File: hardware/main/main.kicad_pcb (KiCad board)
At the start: 2 copper layers, 75 x 75 mm, 62 parts, among them J1 Conn_01x10, J10 Conn_01x02, J11 Conn_01x02, J2 Conn_01x10, J3 Conn_01x02, J4 USB_B_Micro, J5 Conn_01x04, J6 Conn_01x03, J7 Conn_01x02, J8 Conn_01x03, J9 Conn_01x02, K1 G6SU-2, K2 G6SU-2, K3 G6SU-2, K4 G6SU-2, K5 G6SU-2, K6 G6SU-2, K7 G6SU-2, K8 G6SU-2, SW1 Rotary_Encoder_Switch, U1 NCV7726B, U10 SP3485EN, U2 MAX98357A, U3 MOC3043M, U4 SP3485EN, U5 E73-2G4M08S1C-52840, U6 BME680, U7 TPS82130, U8 D203S, U9 UG-2864ASWPG01

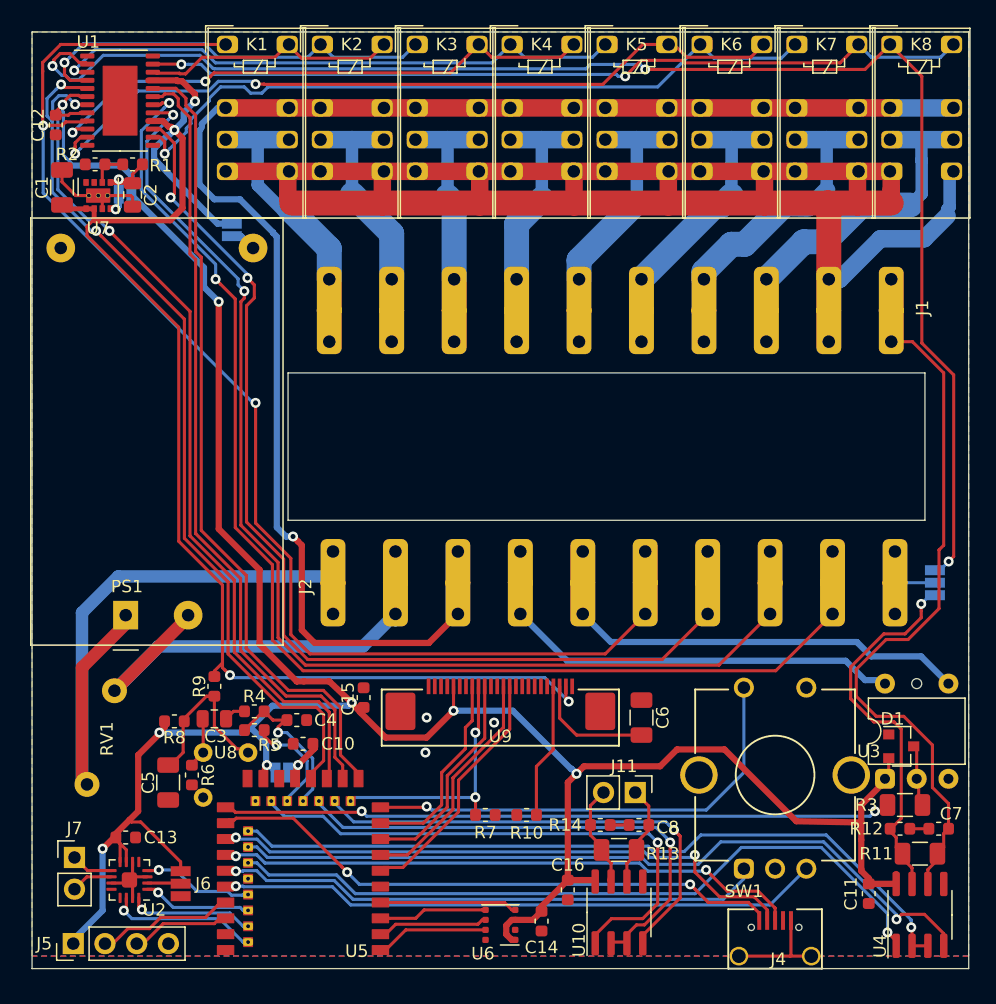
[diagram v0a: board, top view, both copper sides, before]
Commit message: Update main board to use LIN
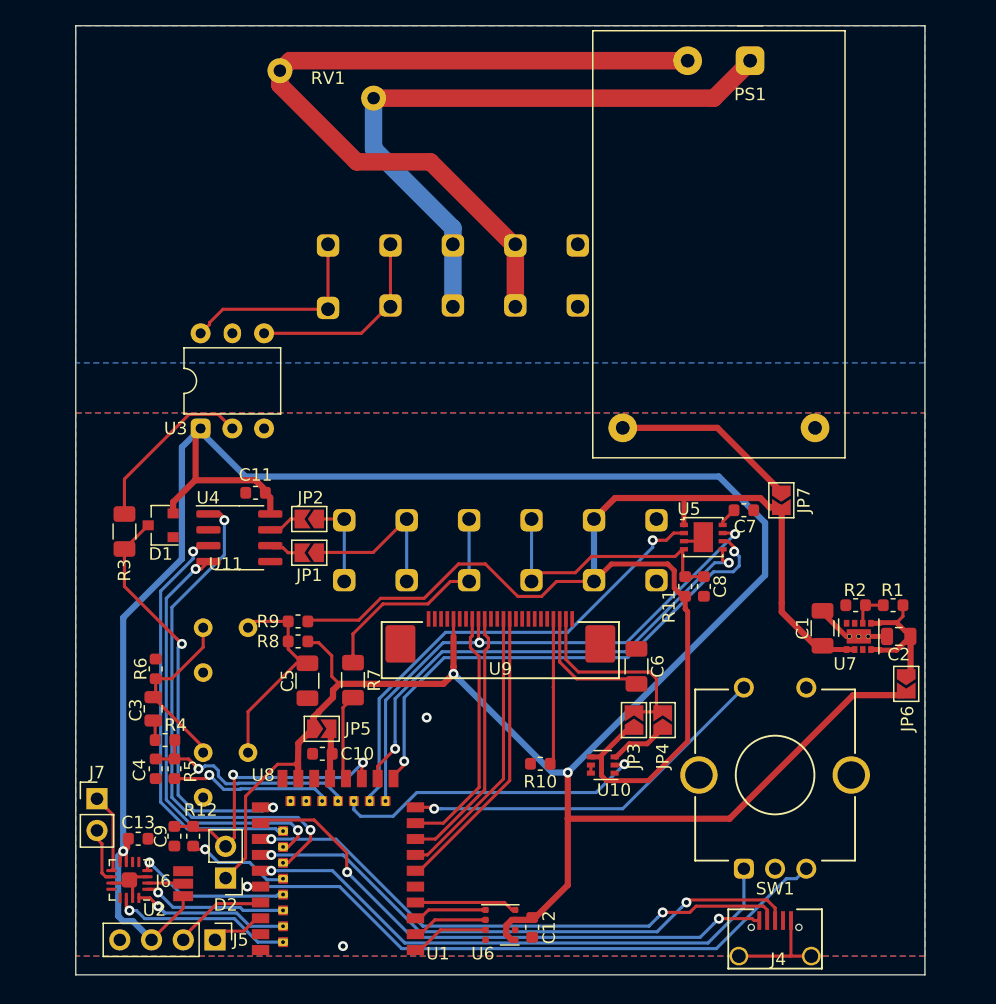
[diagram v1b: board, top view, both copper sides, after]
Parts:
- removed C14, C15, C16: 100n, Capacitor_SMD:C_0603_1608Metric
- removed J10, J3, J9: Conn_01x02, RoomControl:Jumper2
- removed J11: Conn_01x02, Connector_PinHeader_2.54mm:PinHeader_1x02_P2.54mm_Vertical
- removed J8: Conn_01x03, RoomControl:Jumper3
- removed K1, K2, K3, K4, K5, K6, K7, K8: G6SU-2, RoomControl:Relay_DPDT_Omron_G6SU-2
- removed R13: 120R, Resistor_SMD:R_1206_3216Metric
- removed R14: 120R, Resistor_SMD:R_0603_1608Metric
- removed the U1 at (69.5, 68.0)
- added C9: 100n, Capacitor_SMD:C_0603_1608Metric, F.Cu at (73.9, 126.9)
- added D2: D_Photo, Connector_PinHeader_2.54mm:PinHeader_1x02_P2.54mm_Vertical, F.Cu at (78.0, 130.2)
- added JP1: SolderJumper_2_Open, RoomControl:Jumper2Triangular, F.Cu at (84.7, 104.2)
- added JP2: SolderJumper_2_Open, RoomControl:Jumper2Triangular, F.Cu at (84.7, 101.5)
- added JP3: SolderJumper_2_Open, RoomControl:Jumper2Triangular, F.Cu at (110.7, 117.6)
- added JP4: SolderJumper_2_Open, RoomControl:Jumper2Triangular, F.Cu at (113.0, 117.6)
- added JP5: SolderJumper_2_Open, RoomControl:Jumper2Triangular, F.Cu at (85.7, 118.3)
- added JP6: SolderJumper_2_Open, RoomControl:Jumper2Triangular, F.Cu at (132.5, 114.7)
- added JP7: SolderJumper_2_Open, RoomControl:Jumper2Triangular, F.Cu at (122.5, 100.0)
- added U11: D203S, RoomControl:D203S, F.Cu at (78.0, 112.0)
- added U5: NCV7428MW, Package_DFN_QFN:DFN-8-1EP_3x3mm_P0.65mm_EP1.55x2.4mm, F.Cu at (116.2, 103.0)
- C8: value 100n -> 1n
- J1: value Conn_01x10 -> Conn_01x06; footprint RoomControl:WAGO-236-410 -> RoomControl:Wago_236-406; moved to B.Cu
- J2: value Conn_01x10 -> Conn_01x05; footprint RoomControl:WAGO-236-410 -> RoomControl:Wago_236-405; moved to B.Cu
- PS1: footprint Converter_ACDC:Converter_ACDC_HiLink_HLK-PMxx -> RoomControl:Converter_ACDC_HiLink_HLK-PMxx
- R11: value 120R -> 1k; footprint Resistor_SMD:R_1206_3216Metric -> Resistor_SMD:R_0603_1608Metric
- R12: value 120R -> 100k
- R7: value 33k -> 100k; footprint Resistor_SMD:R_0603_1608Metric -> Resistor_SMD:R_1206_3216Metric
- U10: value SP3485EN -> DCX114YU; footprint Package_SO:SOIC-8_3.9x4.9mm_P1.27mm -> Package_TO_SOT_SMD:SOT-363_SC-70-6
- moved C12 74.7 mm to (102.5, 134.2)
- moved C2 70.8 mm to (131.9, 110.9), turned to 180 degrees
- moved C1 70.4 mm to (125.8, 110.2)
- moved R1 70.4 mm to (131.4, 108.4)
- moved R2 70.4 mm to (128.4, 108.4)
- moved U7 70.4 mm to (128.7, 110.9)
- moved PS1 66.9 mm to (120.0, 64.8), turned to 270 degrees
- moved R3 66.2 mm to (69.9, 102.5), turned to 90 degrees
- moved U4 62.3 mm to (79.1, 103.0), turned to 0 degrees
- moved D1 61.9 mm to (72.8, 102.0), turned to 180 degrees
- moved U3 61.6 mm to (76.0, 94.2)
- moved C11 58.7 mm to (80.4, 99.4), turned to 0 degrees
- moved R12 56.6 mm to (75.4, 126.9), turned to 270 degrees
- moved RV1 55.3 mm to (86.1, 66.7), turned to 180 degrees
- moved J1 48.9 mm to (87.5, 104.0)
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- renumbered U5 to U1
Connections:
- net DET_COMP renamed MD_COMP
- net DET_DS renamed MD_DS
- C7 pad 1: Net-(C7-Pad1) -> GND
- C7 pad 2: A -> Net-(C7-Pad2)
- C8 pad 1: Net-(C8-Pad1) -> GND
- C8 pad 2: Net-(C8-Pad2) -> LIN
- D1 pad 3: Net-(D1-Pad3) -> H
- J1 pad 1: A -> RS485_B
- J1 pad 2: L2 -> RS485_A
- J1 pad 3: S1 -> IN
- J1 pad 4: S2 -> LIN
- J1 pad 5: S3 -> +12V
- J1 pad 6: S4 -> GND
- J2 pad 1: L -> H1
- J2 pad 2: N -> H2
- J2 pad 3: PE -> L
- J2 pad 4: H1 -> N
- J2 pad 5: H2 -> PE
- J5 pad 1: +3V3 -> SWDCLK
- J5 pad 3: SWDCLK -> +3V3
- R11 pad 1: B -> LIN
- R11 pad 2: A -> +12V
- R12 pad 1: B -> BS_COMP
- R12 pad 2: Net-(C7-Pad1) -> BS_DS
- R3 pad 2: Net-(D1-Pad3) -> Net-(R3-Pad2)
- R7 pad 1: DISP_RES -> IN
- R7 pad 2: GND -> IN_P
- U1 pad 11: R_SCLK -> LIN_TX
- U1 pad 12: DISP_RES -> RESET
- U1 pad 13: R_CS -> LIN_RX
- U1 pad 14: RS485_2_TX -> LIN_EN
- U1 pad 15: R_MISO -> BS_COMP
- U1 pad 16: RS485_2_DE -> EN_12V
- U1 pad 17: R_MOSI -> IN_P
- U1 pad 22: RS485_2_RX -> Net-(U1-Pad22)
- U1 pad 34: Net-(U5-Pad34) -> BS_DS
- U10 pad 1: RS485_2_RX -> GND
- U10 pad 2: RS485_2_DE -> EN_12V
- U10 pad 3: RS485_2_DE -> Net-(JP4-Pad1)
- U10 pad 4: RS485_2_TX -> +12V
- U10 pad 5: GND -> Net-(U10-Pad5)
- U10 pad 6: Net-(C8-Pad2) -> Net-(U10-Pad5)
- U2 pad 6: GND -> Net-(U2-Pad6)
- U3 pad 2: Net-(D1-Pad3) -> Net-(R3-Pad2)
- U4 pad 6: A -> Net-(JP1-Pad2)
- U4 pad 7: B -> Net-(JP2-Pad2)
- U9 pad 23: +12V -> Net-(JP3-Pad2)
- U9 pad 9: DISP_RES -> RESET
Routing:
- net L2: track 143.2 -> 0.00 mm
- net PE: track 119.9 -> 0.00 mm, vias 1 -> 0
- net R1: track 118.7 -> 0.00 mm, vias 3 -> 0
- net R9: track 103.5 -> 0.00 mm, vias 2 -> 0
- net R12: track 97.8 -> 0.00 mm, vias 2 -> 0
- net R11: track 91.4 -> 0.00 mm, vias 2 -> 0
- net R10: track 82.0 -> 0.00 mm, vias 2 -> 0
- net R_MOSI: track 69.4 -> 0.00 mm, vias 2 -> 0
- net R_MISO: track 68.5 -> 0.00 mm, vias 2 -> 0
- net R2: track 66.9 -> 0.00 mm, vias 2 -> 0
- net R_SCLK: track 65.2 -> 0.00 mm
- net R_CS: track 64.2 -> 0.00 mm
- net R4: track 61.5 -> 0.00 mm, vias 2 -> 0
- net R3: track 58.3 -> 0.00 mm, vias 1 -> 0
- net A: track 55.1 -> 0.00 mm
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- added copper zone on B.Cu, net PE
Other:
- board size 75 x 75 mm -> 68 x 76 mm
- net class HiVolt removed
- net class Mains added: clearance 1, trace_width 0.25, via_dia 0.8, via_drill 0.4
- net class PE removed
- board text added: "12V"
- board text added: "A"
- board text added: "B"
- board text added: "GND"
- board text added: "H"
- board text added: "IN"
- board text added: "L"
- board text added: "LIN"
- board text added: "N"
- board text added: "PE"
- board text added: "RS485"

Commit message: Add backup battery and 32768Hz crystal
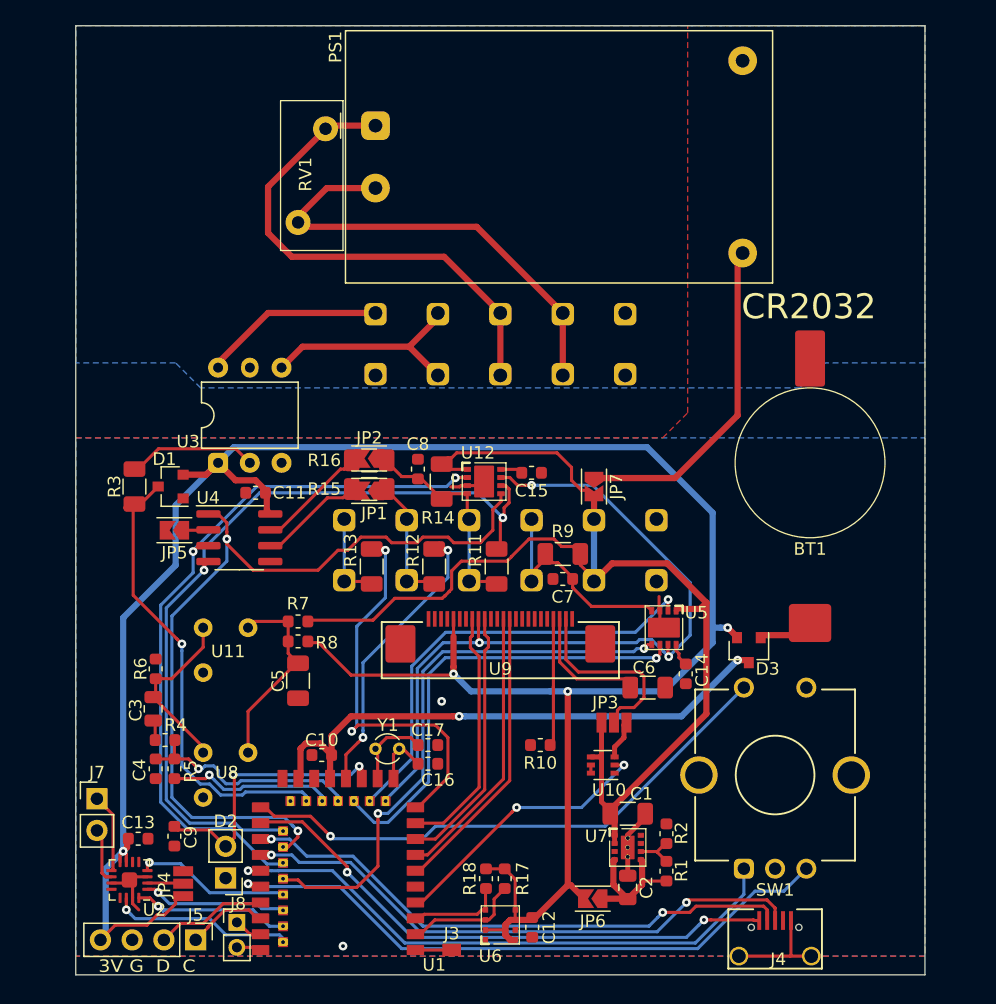
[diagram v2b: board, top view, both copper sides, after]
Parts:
- removed J6: Conn_01x03, RoomControl:Jumper3
- removed the R11 at (114.8, 106.9)
- added BT1: Battery_Cell, RoomControl:Battery_2032, F.Cu at (124.8, 97.0)
- added C14: 100n, Capacitor_SMD:C_0603_1608Metric, F.Cu at (114.8, 113.9)
- added C15: 100n, Capacitor_SMD:C_0603_1608Metric, F.Cu at (102.5, 97.8)
- added C16: 12p, Capacitor_SMD:C_0603_1608Metric, F.Cu at (94.2, 121.1)
- added C17: 12p, Capacitor_SMD:C_0603_1608Metric, F.Cu at (94.2, 119.6)
- added D3: BAS40-05/BAT54C, Package_TO_SOT_SMD:SOT-23, F.Cu at (119.9, 112.0)
- added J3: Conn_01x01, RoomControl:Pad, F.Cu at (96.1, 136.0)
- added J8: Conn_01x02, Connector_PinHeader_2.00mm:PinHeader_1x02_P2.00mm_Vertical, F.Cu at (78.9, 133.8)
- added R13: 33k, Resistor_SMD:R_1206_3216Metric, F.Cu at (89.7, 105.3)
- added R14: 1k, Resistor_SMD:R_1206_3216Metric, F.Cu at (95.3, 98.5)
- added R15: 120R, Resistor_SMD:R_1206_3216Metric, F.Cu at (89.5, 99.1)
- added R16: 120R, Resistor_SMD:R_1206_3216Metric, F.Cu at (89.5, 96.8)
- added R17: 4k7, Resistor_SMD:R_0603_1608Metric, F.Cu at (100.3, 130.3)
- added R18: 4k7, Resistor_SMD:R_0603_1608Metric, F.Cu at (98.8, 130.3)
- added R7: 33k, Resistor_SMD:R_0603_1608Metric, F.Cu at (83.8, 109.7)
- added U12: NCV7428MW3, RoomControl:On_NCV7428MW, F.Cu at (98.7, 98.5)
- added Y1: 32768Hz, Crystal:Crystal_DS26_D2.0mm_L6.0mm_Vertical, F.Cu at (91.9, 119.9)
- C1, C5: value 10u/25V/7XR -> 10u/25V/X7R
- C2, C3: value 22u -> 22u/16V
- C6: value 10u/25V -> 10u/25V/X7R
- C7: value 100n -> 1n
- D1: value BAT54S -> BAS40-04/BAT54S
- JP1, JP2, JP5, JP6, JP7: footprint RoomControl:Jumper2Triangular -> RoomControl:Jumper2
- JP3, JP4: value SolderJumper_2_Open -> SolderJumper_3_Open; footprint RoomControl:Jumper2Triangular -> RoomControl:Jumper3
- PS1: footprint RoomControl:Converter_ACDC_HiLink_HLK-PMxx -> RoomControl:HiLink_HLK-PMxx
- R11: renamed from R7; value 100k -> 33k
- R12: value 100k -> 33k; footprint Resistor_SMD:R_0603_1608Metric -> Resistor_SMD:R_1206_3216Metric
- R6: value 47k -> 33k
- R8: value 33k -> 10k
- R9: value 33k -> 1k; footprint Resistor_SMD:R_0603_1608Metric -> Resistor_SMD:R_1206_3216Metric
- SW1: value Rotary_Encoder_Switch -> PEC12R-4217F-S0024; footprint RoomControl:ALPS-BOURNS-EC12 -> RoomControl:Bourns_PEC12R
- U3: footprint RoomControl:MOC3043 -> RoomControl:On_MOC3043
- U4: value SP3485EN -> SP3485
- U5: value NCV7428MW -> NCV7428MW3; footprint Package_DFN_QFN:DFN-8-1EP_3x3mm_P0.65mm_EP1.55x2.4mm -> RoomControl:On_NCV7428MW
- U6: footprint Package_LGA:Bosch_LGA-8_3x3mm_P0.8mm_ClockwisePinNumbering -> RoomControl:Bosch_BME680
- U7: footprint RoomControl:TPS82130 -> RoomControl:Texas_TPS82130
- moved JP4 40.6 mm to (74.6, 130.7), turned to 180 degrees
- moved PS1 30.4 mm to (90.0, 70.0), turned to 0 degrees
- moved JP6 30.4 mm to (107.4, 131.9), turned to 180 degrees
- moved C2 29.6 mm to (110.2, 131.0), turned to 90 degrees
- moved R12 29.0 mm to (94.7, 105.3), turned to 90 degrees
- moved R1 28.0 mm to (113.3, 129.7), turned to 90 degrees
- moved U7 25.1 mm to (110.2, 127.8), turned to 0 degrees
- moved C8 24.8 mm to (93.4, 97.5)
- moved J2 24.4 mm to (110.0, 87.5), turned to 90 degrees
- moved R2 23.8 mm to (113.3, 126.7), turned to 90 degrees
- moved R9 21.9 mm to (105.0, 104.3), turned to 0 degrees
- moved C1 21.5 mm to (110.2, 125.1), turned to 0 degrees
- moved JP5 19.8 mm to (73.9, 102.4), turned to 180 degrees
- moved C7 15.5 mm to (105.0, 106.3)
- moved JP7 15.0 mm to (107.5, 98.9)
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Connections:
- net BME_MOSI renamed BME_SDA
- net BME_SCK renamed BME_SCL
- C10 pad 1: GND -> Net-(C10-Pad1)
- C10 pad 2: Net-(C10-Pad2) -> GND
- C7 pad 1: GND -> LIN
- C7 pad 2: Net-(C7-Pad2) -> GND
- C8 pad 1: GND -> IN1_LIN2_RS485_B
- C8 pad 2: LIN -> GND
- C9 pad 2: BS_COMP -> BS
- D2 pad 1: +3V3 -> GND
- D2 pad 2: BS_COMP -> BS
- J1 pad 1: RS485_B -> IN3
- J1 pad 2: RS485_A -> IN2_RS485_A
- J1 pad 3: IN -> IN1_LIN2_RS485_B
- J2 pad 1: H1 -> PE
- J2 pad 2: H2 -> N
- J2 pad 4: N -> H2
- J2 pad 5: PE -> H1
- J5 pad 3: +3V3 -> GND
- J5 pad 4: GND -> +3V3
- JP1 pad 1: RS485_A -> IN2_RS485_A
- JP2 pad 1: RS485_B -> IN1_LIN2_RS485_B
- JP4 pad 1: Net-(JP4-Pad1) -> +3V3
- JP4 pad 2: Net-(JP3-Pad2) -> Net-(JP4-Pad2)
- JP5 pad 1: +3V3 -> Net-(JP5-Pad1)
- JP5 pad 2: Net-(C10-Pad2) -> GND
- R11 pad 1: IN -> IN1_LIN2_RS485_B
- R11 pad 2: IN_P -> IN1_LIN2_RS485_TX
- R12 pad 1: BS_COMP -> IN2_RS485_A
- R12 pad 2: BS_DS -> IN2_P
- R8 pad 1: Net-(C5-Pad1) -> +3V3
- R8 pad 2: +3V3 -> Net-(C5-Pad1)
- R9 pad 1: +12V -> LIN
- R9 pad 2: Net-(C5-Pad1) -> +12V
- U1 pad 1: BME_CSB -> Net-(J3-Pad1)
- U1 pad 10: SWITCH -> IN3_P
- U1 pad 11: LIN_TX -> Net-(C16-Pad1)
- U1 pad 13: LIN_RX -> Net-(C17-Pad1)
- U1 pad 15: BS_COMP -> BS
- U1 pad 16: EN_12V -> LIN_TX
- U1 pad 17: IN_P -> IN2_P
- U1 pad 19: Net-(C10-Pad2) -> Net-(C10-Pad1)
- U1 pad 22: Net-(U1-Pad22) -> H
- U1 pad 23: +3V3 -> Net-(C10-Pad1)
- U1 pad 26: H -> SWITCH
- U1 pad 28: RS485_DE -> IN1_LIN2_RS485_TX
- U1 pad 30: RS485_TX -> LIN2_RS485_RX
- U1 pad 32: RS485_RX -> LIN2_EN_RS485_DE
- U1 pad 34: BS_DS -> LIN_RX
- U1 pad 4: BME_MISO -> EN_12V
- U10 pad 3: Net-(JP4-Pad1) -> Net-(JP3-Pad3)
- U2 pad 2: Net-(J6-Pad2) -> Net-(JP4-Pad2)
- U4 pad 1: RS485_RX -> LIN2_RS485_RX
- U4 pad 2: RS485_DE -> Net-(JP5-Pad1)
- U4 pad 3: RS485_DE -> LIN2_EN_RS485_DE
- U4 pad 4: RS485_TX -> IN1_LIN2_RS485_TX
- U5 pad 8: Net-(C7-Pad2) -> Net-(C14-Pad2)
- U6 pad 2: BME_CSB -> +3V3
- U6 pad 5: BME_MISO -> +3V3
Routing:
- net LIN2_RS485_RX: track 0.00 -> 66.6 mm, vias 0 -> 2
- net IN1_LIN2_RS485_TX: track 0.00 -> 64.8 mm, vias 0 -> 2
- net LIN2_EN_RS485_DE: track 0.00 -> 58.9 mm, vias 0 -> 2
- net +3V3: track 244.7 -> 191.3 mm, vias 3 -> 4
- net Net-(C10-Pad1): track 0.00 -> 45.2 mm, vias 0 -> 2
- net RS485_RX: track 41.5 -> 0.00 mm, vias 2 -> 0
- net RS485_TX: track 34.3 -> 0.00 mm, vias 2 -> 0
- net RS485_DE: track 33.3 -> 0.00 mm, vias 1 -> 0
- net IN3_P: track 0.00 -> 32.1 mm, vias 0 -> 2
- net N: track 63.1 -> 36.7 mm
- net IN2_P: track 0.00 -> 24.0 mm, vias 0 -> 2
- net BS_COMP: track 23.1 -> 0.00 mm, vias 2 -> 0
- net BS: track 0.00 -> 22.3 mm, vias 0 -> 2
- net IN: track 18.3 -> 0.00 mm
- net IN1_LIN2_RS485_B: track 0.00 -> 17.9 mm
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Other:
- net class Default: via_dia 0.8 -> 0.7; via_drill 0.4 -> 0.3
- board text added: "1"
- board text added: "2"
- board text added: "3"
- board text added: "3V G D C"
- board text added: "CR2032"
- board text removed: "IN"
- board text removed: "RS485"

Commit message: New speaker and pir sensor lens
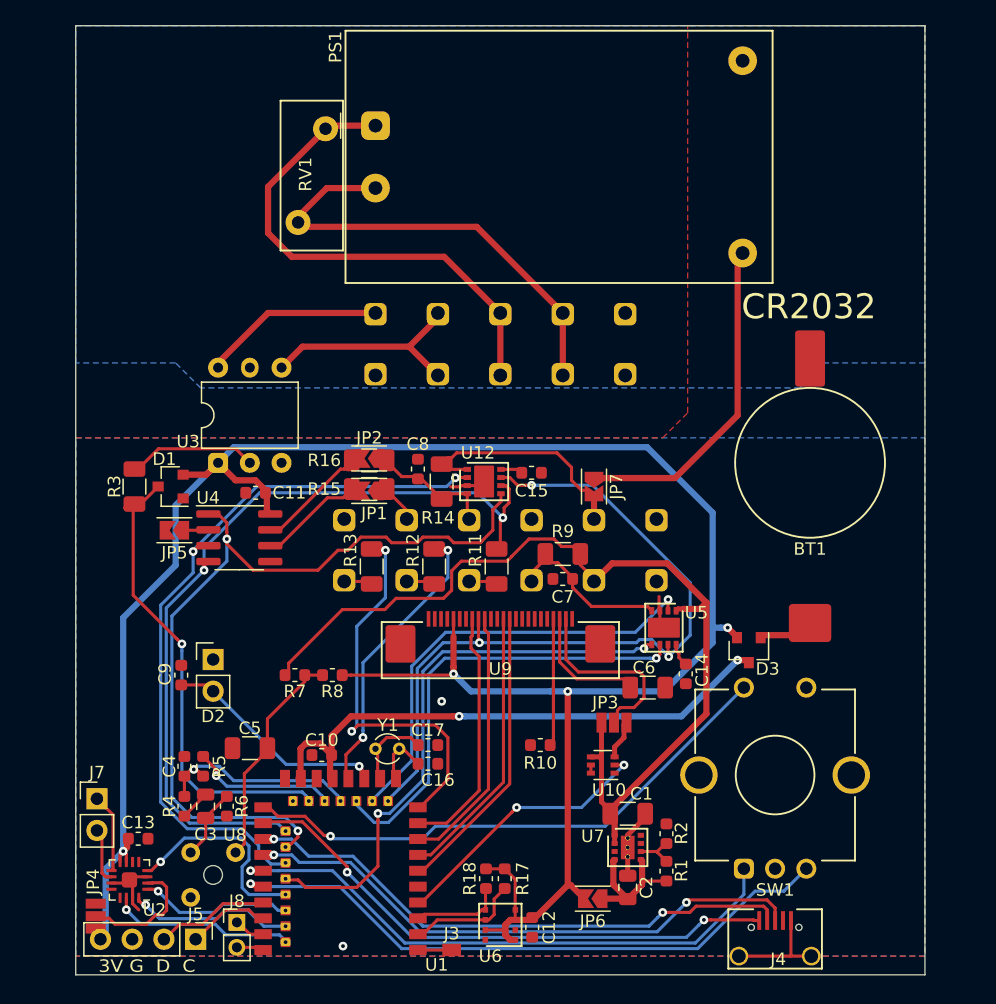
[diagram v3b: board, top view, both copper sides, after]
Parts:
- removed U11: D203S, RoomControl:D203S
- moved D2 17.5 mm to (77.0, 112.8), turned to 0 degrees
- moved C9 12.9 mm to (74.5, 114.0), turned to 270 degrees
- moved R6 12.4 mm to (78.1, 124.5), turned to 90 degrees
- moved C3 8.86 mm to (76.4, 124.5), turned to 270 degrees
- moved U8 8.06 mm to (77.0, 130.0)
- moved JP4 7.47 mm to (67.6, 133.3)
- moved C5 6.63 mm to (80.0, 119.8), turned to 180 degrees
- moved R4 5.52 mm to (74.7, 124.5), turned to 90 degrees
- moved R7 4.31 mm to (83.5, 114.0), turned to 180 degrees
- moved R8 3.85 mm to (86.5, 114.0)
- moved C4 2.31 mm to (74.7, 121.3), turned to 270 degrees
- moved R5 2.31 mm to (76.2, 121.3), turned to 90 degrees
- moved U1 0.20 mm to (87.2, 130.3)
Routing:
- net +3V3: track 191.3 -> 180.4 mm
- net Net-(C3-Pad2): track 14.1 -> 5.69 mm
- net Net-(JP4-Pad2): track 2.88 -> 10.00 mm
- net IN2_RS485_A: track 11.4 -> 5.97 mm
- net LIN: track 19.0 -> 14.0 mm
- net IN3: track 7.34 -> 2.34 mm
- net IN1_LIN2_RS485_B: track 17.9 -> 12.9 mm
- net BS: track 22.3 -> 18.0 mm, vias 2 -> 1
- net SP_EN: track 12.5 -> 16.5 mm
- net Net-(C5-Pad1): track 15.9 -> 17.9 mm
- net MD_COMP: track 18.4 -> 16.6 mm
- net MD_DS: track 13.3 -> 11.5 mm
- net +12V: track 97.1 -> 96.1 mm
- net Net-(C3-Pad1): track 1.63 -> 2.43 mm
- net SP_BCLK: track 12.6 -> 13.2 mm
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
